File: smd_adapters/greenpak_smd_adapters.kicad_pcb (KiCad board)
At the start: 2 copper layers, 86.1 x 67.3 mm, 12 parts

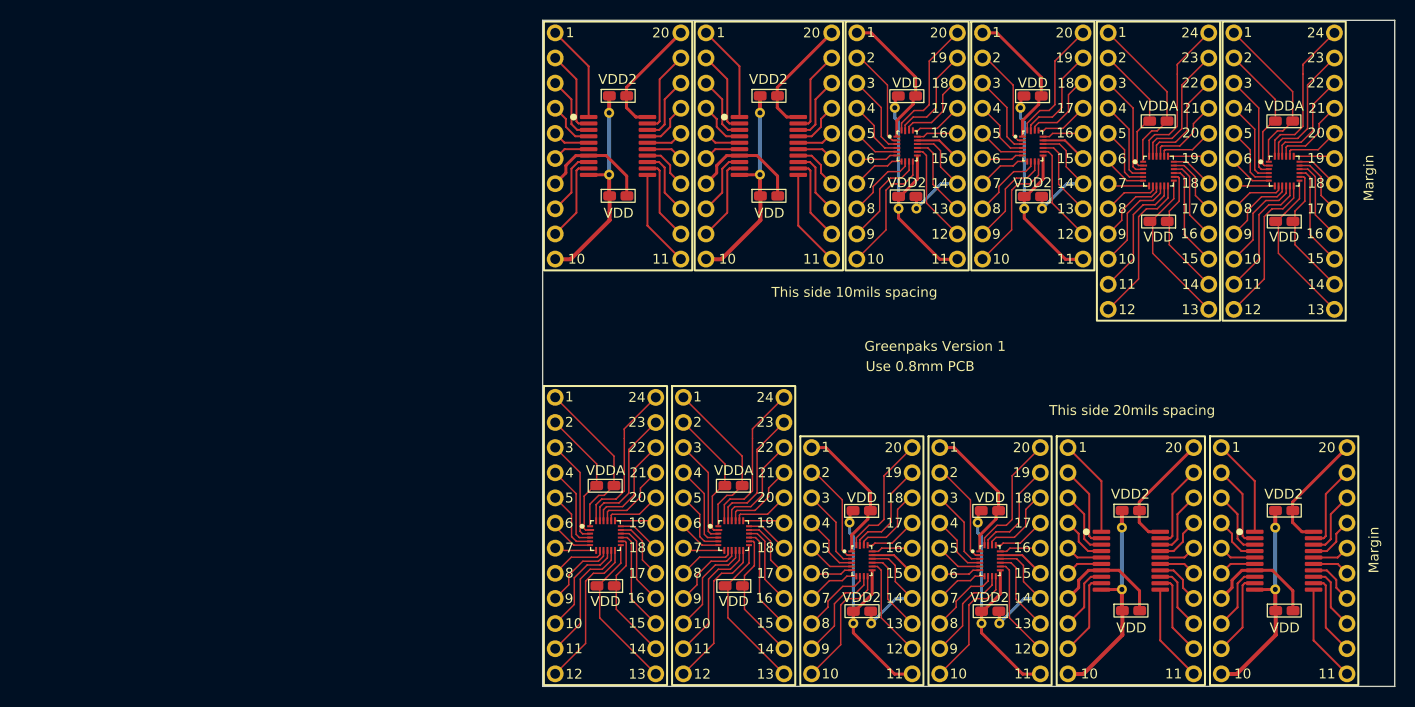
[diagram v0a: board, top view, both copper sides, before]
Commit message: Working in progress on the QWIIC greenpack adapter.
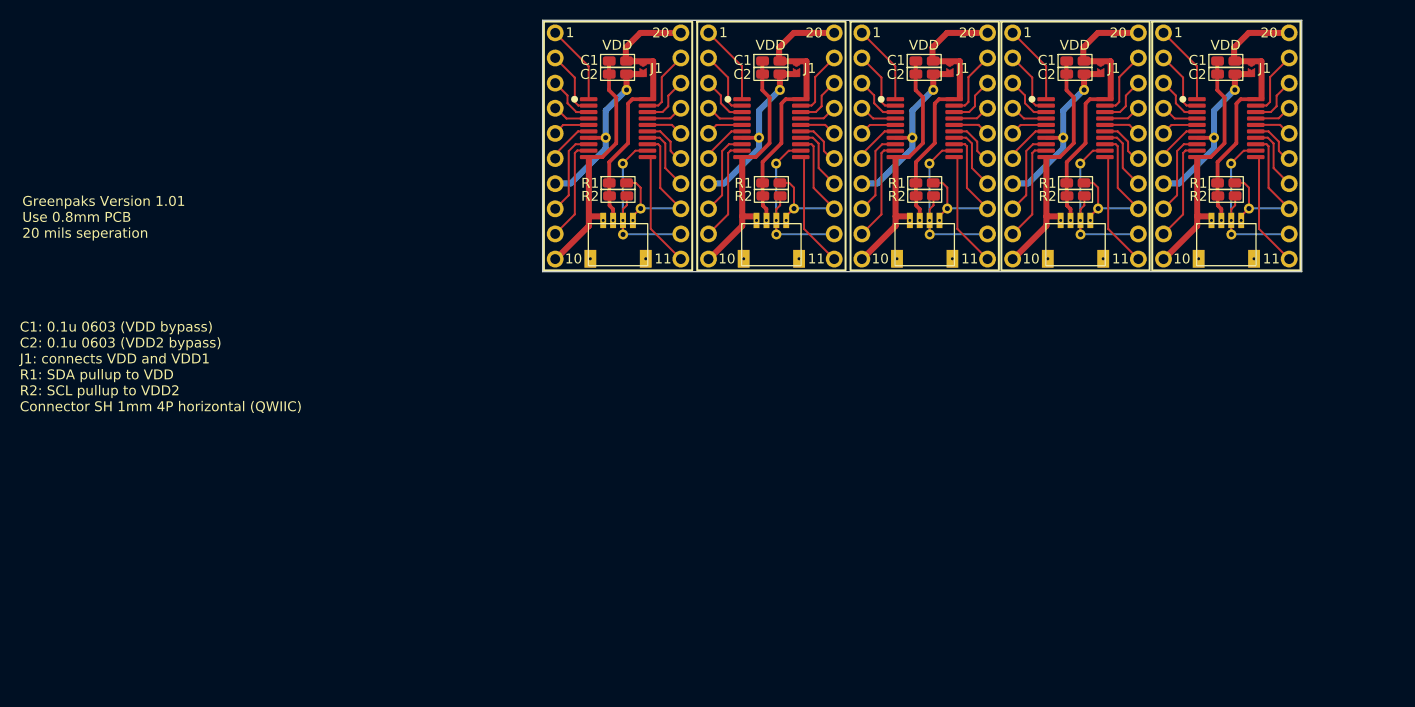
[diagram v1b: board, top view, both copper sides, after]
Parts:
- removed the REF** at (79.4, 78.1)
- removed the REF** at (105.3, 80.6)
- removed the REF** at (118.2, 80.6)
- removed the REF** at (92.3, 78.1)
- removed the REF** at (135.3, 41.3)
- removed the REF** at (122.6, 38.7)
- removed the REF** at (148.0, 41.3)
- removed the REF** at (95.9, 38.7)
- removed the REF** at (109.9, 38.7)
- removed the REF** at (80.6, 38.7)
- removed the REF** at (132.5, 80.6)
- removed the REF** at (148.0, 80.6)
- added REF**: GREENPAK-SMD-ADAPTER-TSSOP-20-QWIIC, greenpack_smd_adapters:GREENPAK-SMD-ADAPTER-TSSOP-20-QWIIC, F.Cu at (126.9, 38.7)
- added REF**: GREENPAK-SMD-ADAPTER-TSSOP-20-QWIIC, greenpack_smd_adapters:GREENPAK-SMD-ADAPTER-TSSOP-20-QWIIC, F.Cu at (142.1, 38.7)
- added REF**: GREENPAK-SMD-ADAPTER-TSSOP-20-QWIIC, greenpack_smd_adapters:GREENPAK-SMD-ADAPTER-TSSOP-20-QWIIC, F.Cu at (111.6, 38.7)
- added REF**: GREENPAK-SMD-ADAPTER-TSSOP-20-QWIIC, greenpack_smd_adapters:GREENPAK-SMD-ADAPTER-TSSOP-20-QWIIC, F.Cu at (96.1, 38.7)
- added REF**: GREENPAK-SMD-ADAPTER-TSSOP-20-QWIIC, greenpack_smd_adapters:GREENPAK-SMD-ADAPTER-TSSOP-20-QWIIC, F.Cu at (80.6, 38.7)
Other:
- board size 86.1 x 67.3 mm -> 76.7 x 25.4 mm
- board text added: "C1: 0.1u 0603 (VDD bypass) C2: 0.1u 0603 (VDD2 bypass) J1: connects VDD and VDD1 R1: SDA pullup to VDD R2: SCL pullup to VDD2 Connector SH 1mm 4P horizontal (QWIIC)"
- board text added: "Greenpaks Version 1.01 Use 0.8mm PCB 20 mils seperation"
- board text removed: "Greenpaks Version 1"
- board text removed: "Margin"
- board text removed: "This side 10mils spacing"
- board text removed: "This side 20mils spacing"
- board text removed: "Use 0.8mm PCB"

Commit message: Finalized the QWIIC adapter layout.
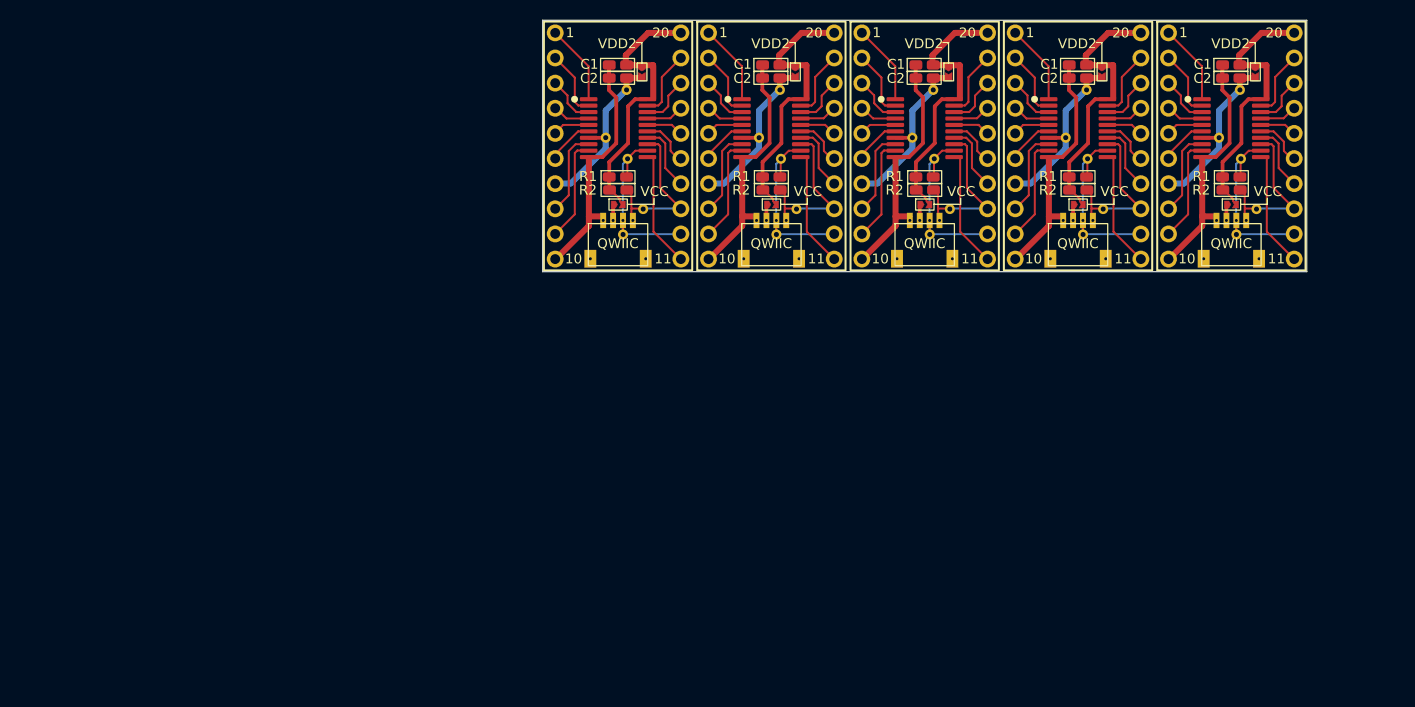
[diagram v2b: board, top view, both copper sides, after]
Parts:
- moved REF** 0.51 mm to (142.6, 38.7)
- moved REF** 0.25 mm to (127.1, 38.7)
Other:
- board size 76.7 x 25.4 mm -> 77.2 x 25.4 mm
- board text added: "C1: 0.1u 0603 (VDD bypass) C2: 0.1u 0603 (VDD2 bypass) R1: SDA pullup to VDD R2: SCL pullup to VDD2 Connector SH 1mm 4P horizontal (QWIIC) VDD2: Connects VDD and VDD2 VCC: Connects QWIIC VCC to VDD."
- board text added: "Greenpaks Version 1.02 Use 0.8mm PCB"
- board text removed: "C1: 0.1u 0603 (VDD bypass) C2: 0.1u 0603 (VDD2 bypass) J1: connects VDD and VDD1 R1: SDA pullup to VDD R2: SCL pullup to VDD2 Connector SH 1mm 4P horizontal (QWIIC)"
- board text removed: "Greenpaks Version 1.01 Use 0.8mm PCB 20 mils seperation"
